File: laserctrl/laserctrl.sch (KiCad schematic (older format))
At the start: 23 parts, among them P0.4 CONN_1, P0.5 CONN_1, P1.17 CONN_1, P1.19 CONN_1, P1.22 CONN_1, P1.25 CONN_1, P25 JTAG, P4.28 CONN_1, P4.29 CONN_1, U1 LPC1769FBD100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

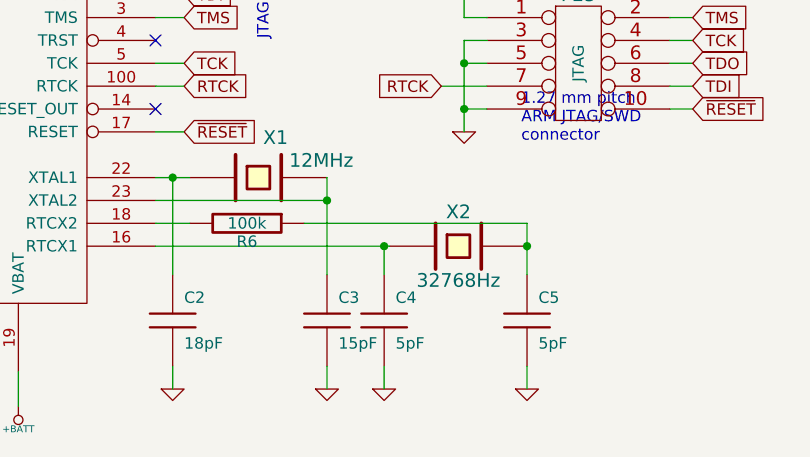
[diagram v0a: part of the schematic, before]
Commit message: Generated the BOM and figured out what parts to buy at ELFA and Mouser
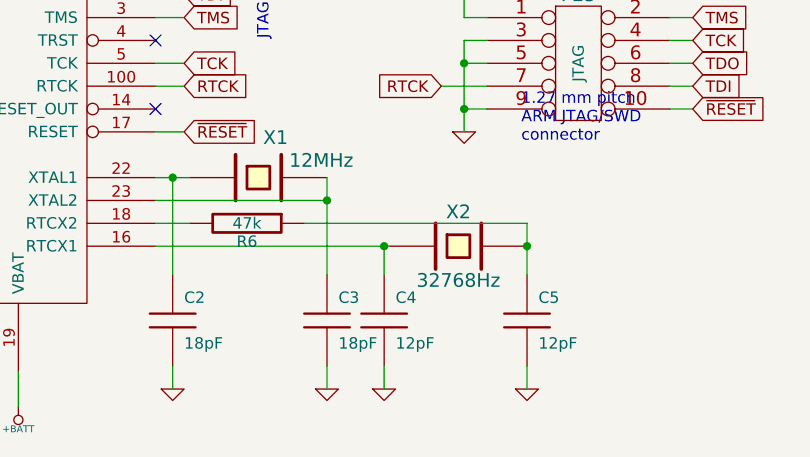
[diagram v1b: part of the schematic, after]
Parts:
- C3: value 15pF -> 18pF
- C4, C5: value 5pF -> 12pF
- R6: value 100k -> 47k
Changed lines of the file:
@@
-EESchema Schematic File Version 2  date 2011-11-28T22:17:03 CET
+EESchema Schematic File Version 2  date 2011-12-03T21:12:32 CET
 LIBS:power
 LIBS:device
@@
 Sheet 1 10
 Title ""
-Date "27 nov 2011"
+Date "3 dec 2011"
 Rev ""
 Comp ""
@@
 P 6325 7075
 F 0 "C5" H 6375 7175 50  0000 L CNN
-F 1 "5pF" H 6375 6975 50  0000 L CNN
+F 1 "12pF" H 6375 6975 50  0000 L CNN
 	1    6325 7075
 	1    0    0    -1
@@
 P 5700 7075
 F 0 "C4" H 5750 7175 50  0000 L CNN
-F 1 "5pF" H 5750 6975 50  0000 L CNN
+F 1 "12pF" H 5750 6975 50  0000 L CNN
 	1    5700 7075
 	1    0    0    -1
@@
 P 5450 7075
 F 0 "C3" H 5500 7175 50  0000 L CNN
-F 1 "15pF" H 5500 6975 50  0000 L CNN
+F 1 "18pF" H 5500 6975 50  0000 L CNN
 	1    5450 7075
 	1    0    0    -1
@@
 P 5100 6650
 F 0 "R6" V 5180 6650 50  0000 C CNN
-F 1 "100k" V 5100 6650 50  0000 C CNN
+F 1 "47k" V 5100 6650 50  0000 C CNN
 	1    5100 6650
 	0    1    1    0

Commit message: Checked footprints and fixed 1 thinko on the ARM and unfucked the transistor foot prints
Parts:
- renumbered P1.19 to P0.27
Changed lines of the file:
@@
-EESchema Schematic File Version 2  date 2011-12-03T21:12:32 CET
+EESchema Schematic File Version 2  date 2011-12-07T22:22:26 CET
 LIBS:power
 LIBS:device
@@
 LIBS:78l00a
 LIBS:conn_11x2
+LIBS:bc807
+LIBS:bc817
 LIBS:laserctrl-cache
 EELAYER 25  0
@@
 Sheet 1 10
 Title ""
-Date "3 dec 2011"
+Date "7 dec 2011"
 Rev ""
 Comp ""
@@
 P2.13
 Text GLabel 9750 4900 0    50   Input ~ 0
-P0.27
+P1.19
 Text GLabel 10800 5000 2    50   Input ~ 0
 P1.4
@@
 $EndComp
 $Comp
-L CONN_1 P1.19
+L CONN_1 P0.27
 U 1 1 4EC15ABB
 P 1750 1300
-F 0 "P1.19" H 1830 1300 40  0000 L CNN
+F 0 "P0.27" H 1830 1300 40  0000 L CNN
 F 1 "CONN_1" H 1750 1355 30  0001 C CNN
 	1    1750 1300
@@
 P1.22
 Text GLabel 2000 1300 2    50   Input ~ 0
-P1.19
+P0.27
 Text GLabel 2000 1400 2    50   Input ~ 0
 P1.17
@@
 P3.26
 Text GLabel 4700 850  0    50   Input ~ 0
-P0.27
+P1.19
 Text GLabel 4800 4350 2    50   Input ~ 0
 P1.25

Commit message: Wired up the watchdog to the new fire feedback signal
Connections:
- net labels added: FireFB
- wire segments 221 -> 222

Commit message: Did some more rev2 schematic changes
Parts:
- removed P0.5: CONN_1, symbol CONN_1
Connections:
- net labels added: SDRESET
- net labels removed: P0.5

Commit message: Completed the schematic changes for rev2 of laserctrl
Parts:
- removed AD4, P0.27, P0.4, P1.17, P1.22, P1.25, P4.28, P4.29, PWM6: CONN_1, symbol CONN_1
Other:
- note added: "Solderpads for testing"
- note removed: "Unused pins terminated\nat solder pads on PCB"
